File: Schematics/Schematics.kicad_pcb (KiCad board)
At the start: 2 copper layers, 8 parts, among them J1 Relay, J2 IR Sensor, J3 BB_I2C, U1 L7805, U2 ATtiny85-20PU

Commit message: An error was correct, and the board was updated. Adjustments are still necessary.
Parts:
- added C2: 0.1u, Capacitor_THT:C_Disc_D3.0mm_W1.6mm_P2.50mm, F.Cu at (120.7, 61.0)
- added C3: 10u, Capacitor_THT:CP_Radial_D5.0mm_P2.00mm, F.Cu at (121.4, 56.1)
- added R2: 100, Resistor_THT:R_Axial_DIN0204_L3.6mm_D1.6mm_P1.90mm_Vertical, F.Cu at (127.3, 54.4)
- added R3: 10k, Resistor_THT:R_Axial_DIN0204_L3.6mm_D1.6mm_P1.90mm_Vertical, F.Cu at (126.3, 61.0)
- C1: footprint Capacitor_THT:CP_Radial_D4.0mm_P1.50mm -> Capacitor_THT:C_Disc_D3.0mm_W1.6mm_P2.50mm
- moved J2 14.8 mm to (116.8, 55.2)
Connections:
- J2 pad 2: VCC -> GND
- J2 pad 3: GND -> Net-(C2-Pad1)

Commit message: The IR circuit was added to the layout.
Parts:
- moved C3 24.1 mm to (113.0, 78.7), turned to 270 degrees
- moved C2 17.9 mm to (119.4, 78.8), turned to 270 degrees
- moved J2 13.6 mm to (114.3, 68.6)
- moved R2 13.6 mm to (114.3, 58.4), turned to 180 degrees
- moved R3 12.1 mm to (114.3, 62.2), turned to 180 degrees
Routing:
- net Net-(C2-Pad1): track 0.00 -> 30.1 mm
- net /IR_Signal: track 8.53 -> 14.8 mm
- net VCC: track 37.7 -> 39.6 mm, vias 1 -> 2
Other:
- board text added: "Any Button"
- board text added: "Battery"
- board text added: "IR Receiver"
- board text added: "Relay"

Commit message: The schematic was updated.
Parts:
- C3: footprint Capacitor_THT:CP_Radial_D5.0mm_P2.00mm -> Capacitor_THT:C_Disc_D3.0mm_W1.6mm_P2.50mm

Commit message: A capacitor value was changed.
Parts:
- C3: value 10u -> 100u

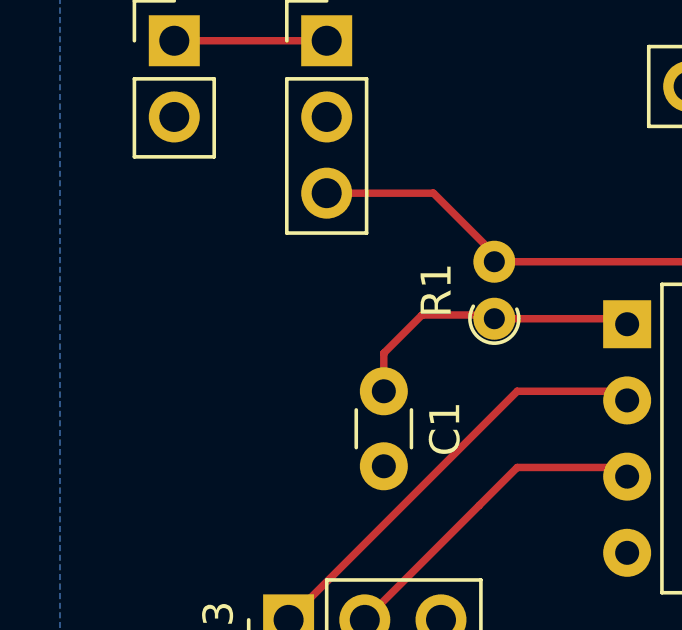
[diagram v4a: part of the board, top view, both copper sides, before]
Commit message: A battery input was added for lower voltages.
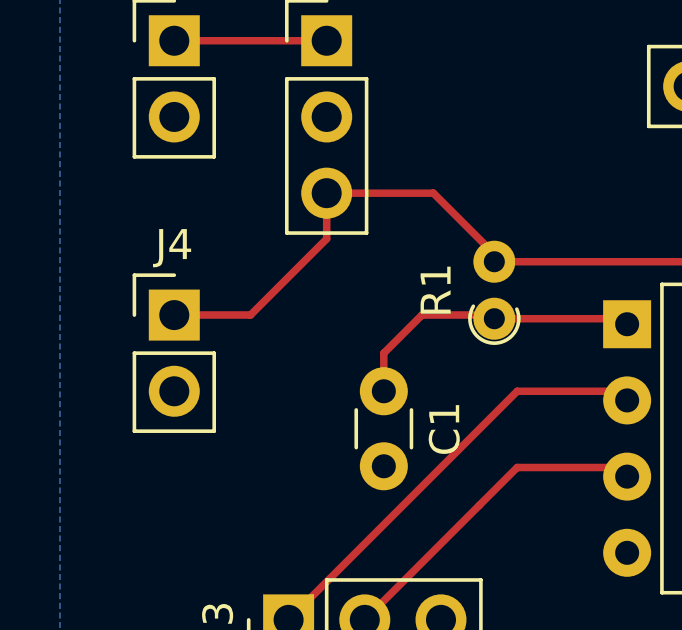
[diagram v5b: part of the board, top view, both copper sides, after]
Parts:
- added J4: Conn_01x02, Connector_PinHeader_2.54mm:PinHeader_1x02_P2.54mm_Vertical, F.Cu at (83.8, 67.3)
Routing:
- net VCC: track 39.6 -> 47.0 mm
